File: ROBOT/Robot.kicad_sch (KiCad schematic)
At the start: 14 parts, among them J1 Conn_02x20_Odd_Even, J2 Conn_01x06, J5 Conn_01x02, U3 AZ1117-3.3

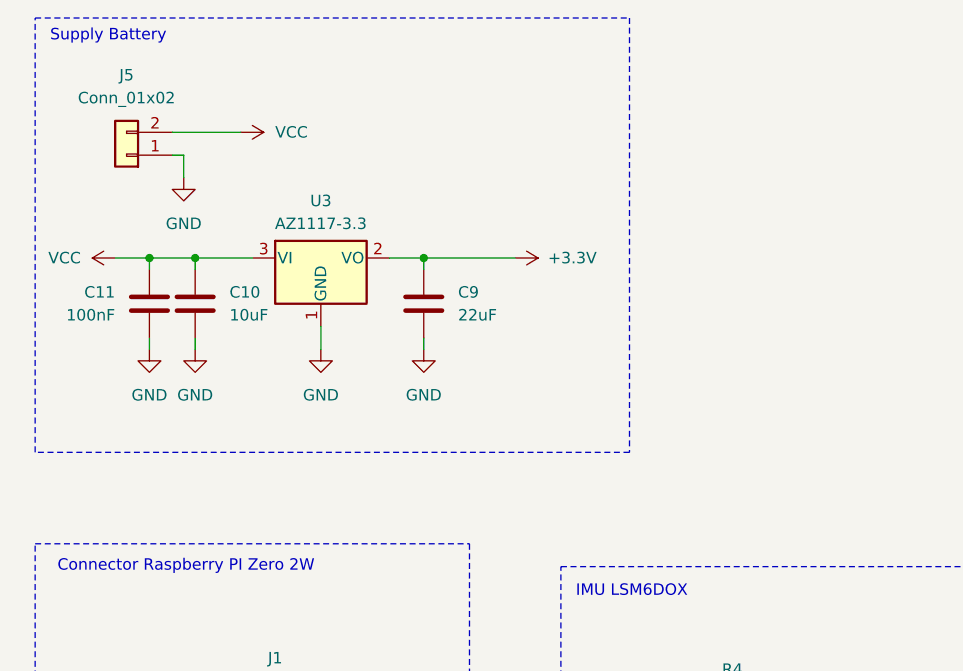
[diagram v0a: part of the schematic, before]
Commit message: add DC-DC BUCK + LED
add DC-DC BUCK + LED
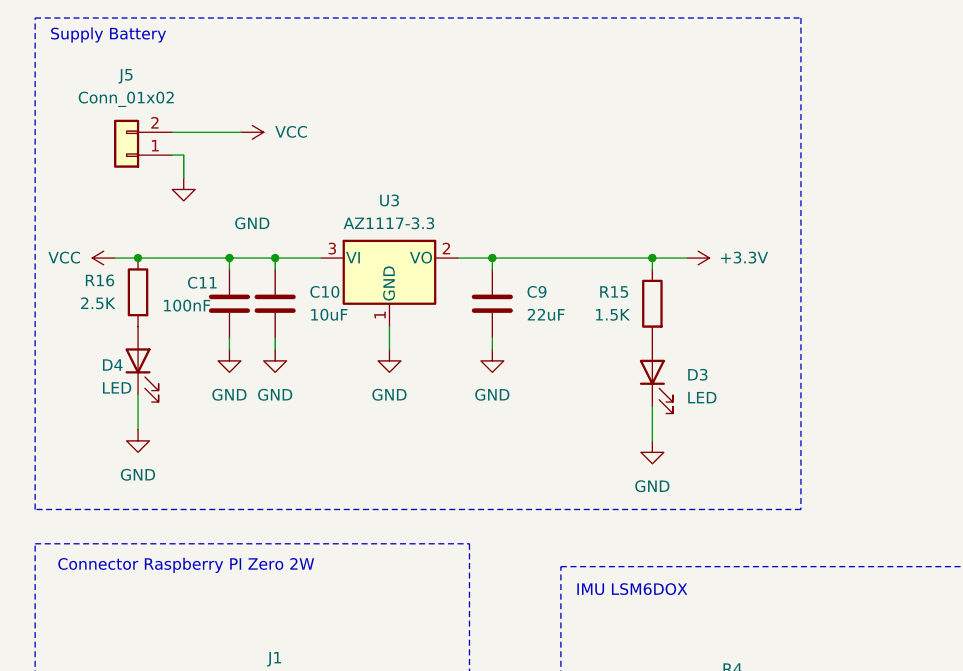
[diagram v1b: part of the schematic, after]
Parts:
- added D3, D4: LED, symbol Device:LED
- added R15: 1.5K, Resistor_SMD:R_0603_1608Metric_Pad0.98x0.95mm_HandSolder, symbol Device:R
- added R16: 2.5K, Resistor_SMD:R_0603_1608Metric_Pad0.98x0.95mm_HandSolder, symbol Device:R
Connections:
- net +3.3V: now also R15.1
- net GND: now also D3.1 (K), D4.1 (K)
- net VCC: now also R16.1
- new net: D3.2 (A), R15.2
- new net: D4.2 (A), R16.2
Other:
- moved on the sheet: C10, C11, C9, U3

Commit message: correction schéma
correction schéma
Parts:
- removed C1, C11, C2: 100nF, Capacitor_SMD:C_0603_1608Metric_Pad1.08x0.95mm_HandSolder, symbol Device:C
- removed C10: 10uF, Capacitor_SMD:C_0603_1608Metric_Pad1.08x0.95mm_HandSolder, symbol Device:C
- removed C9: 22uF, Capacitor_SMD:C_0603_1608Metric_Pad1.08x0.95mm_HandSolder, symbol Device:C
- removed D3, D4: LED, symbol Device:LED
- removed R15: 1.5K, Resistor_SMD:R_0603_1608Metric_Pad0.98x0.95mm_HandSolder, symbol Device:R
- removed R16: 2.5K, Resistor_SMD:R_0603_1608Metric_Pad0.98x0.95mm_HandSolder, symbol Device:R
- removed R3: 10K, Resistor_SMD:R_0603_1608Metric_Pad0.98x0.95mm_HandSolder, symbol Device:R
- removed R4: 0, Resistor_SMD:R_0603_1608Metric_Pad0.98x0.95mm_HandSolder, symbol Device:R
- removed U$2: LSM6DSOX, Adafruit_LSM6DSOX:LGA-14L, symbol Adafruit_LSM6DSOX-eagle-import:LSM6DSOX
- removed U3: AZ1117-3.3, symbol Regulator_Linear:AZ1117-3.3
- added C17, C19, C21: 100nF, Capacitor_SMD:C_0603_1608Metric_Pad1.08x0.95mm_HandSolder, symbol Device:C_Small
- added C18, C20: 220uF, symbol Device:C_Polarized
- added D5, D6: LED, LED_SMD:LED_0603_1608Metric_Pad1.05x0.95mm_HandSolder, symbol Device:LED
- added H1, H2, H3, H4: MountingHole_Pad, symbol Mechanical:MountingHole_Pad
- added J7: Battery, symbol Connector_Generic:Conn_01x02
- J2: value Conn_01x06 -> MCP3208
- J5: value Conn_01x02 -> Battery
- R1: value 10K -> 6.8k
- R2: value 10K -> 1K
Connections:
- net +3.3V: now also R2.1, C17.1
- net DIR_LEFT: now also J1.31 (Pin_31); no longer J1.29 (Pin_29)
- net DIR_RIGHT: now also J1.36 (Pin_36); no longer J1.16 (Pin_16)
- net GND: now also J1.20 (Pin_20), J1.30 (Pin_30), J1.34 (Pin_34), J1.39 (Pin_39), C17.2, C18.2, C19.2, C20.2, C21.2, D5.1 (K), D6.1 (K), H1.1, H2.1, H3.1, H4.1, J7.1 (Pin_1)
- net MOSI: now also J1.19 (Pin_19); no longer J1.40 (Pin_40)
- net SCL_3V3: no longer R2.2
- net SDA_3V3: no longer R1.2
- net STEP_LEFT: now also J1.33 (Pin_33); no longer J1.31 (Pin_31)
- net STEP_RIGHT: now also J1.32 (Pin_32); no longer J1.18 (Pin_18)
- net VCC: now also R1.1, C18.1, C19.1, C20.1, C21.1, J7.2 (Pin_2)
- new net: D6.2 (A), R2.2
- new net: D5.2 (A), R1.2
- no-connect marks 29 -> 21
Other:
- added sheet IMU LSM6DOX (LSM6DOX.kicad_sch)
- note added: "LED"
- note removed: "IMU LSM6DOX"
- moved on the sheet: J1, J2
